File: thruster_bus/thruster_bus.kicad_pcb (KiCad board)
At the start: 2 copper layers, 35.4 x 38.1 mm, 10 parts, among them P1 CONN_01X03, P2 CONN_01X03, P3 CONN_01X03, P4 CONN_01X05, P5 CONN_01X03, P6 CONN_01X03

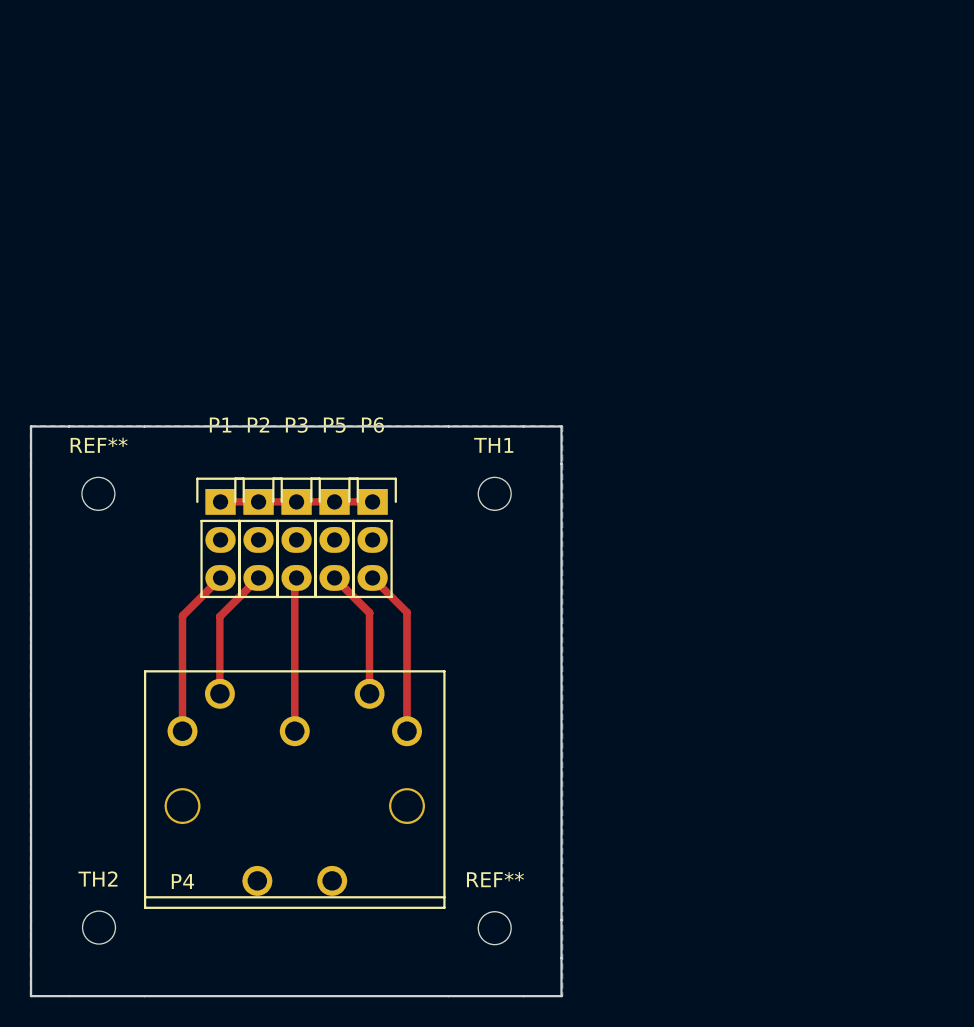
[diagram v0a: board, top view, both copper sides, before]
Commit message: Changed thruster bus pcb to use 6 pin cui connector and to use 5v and GND
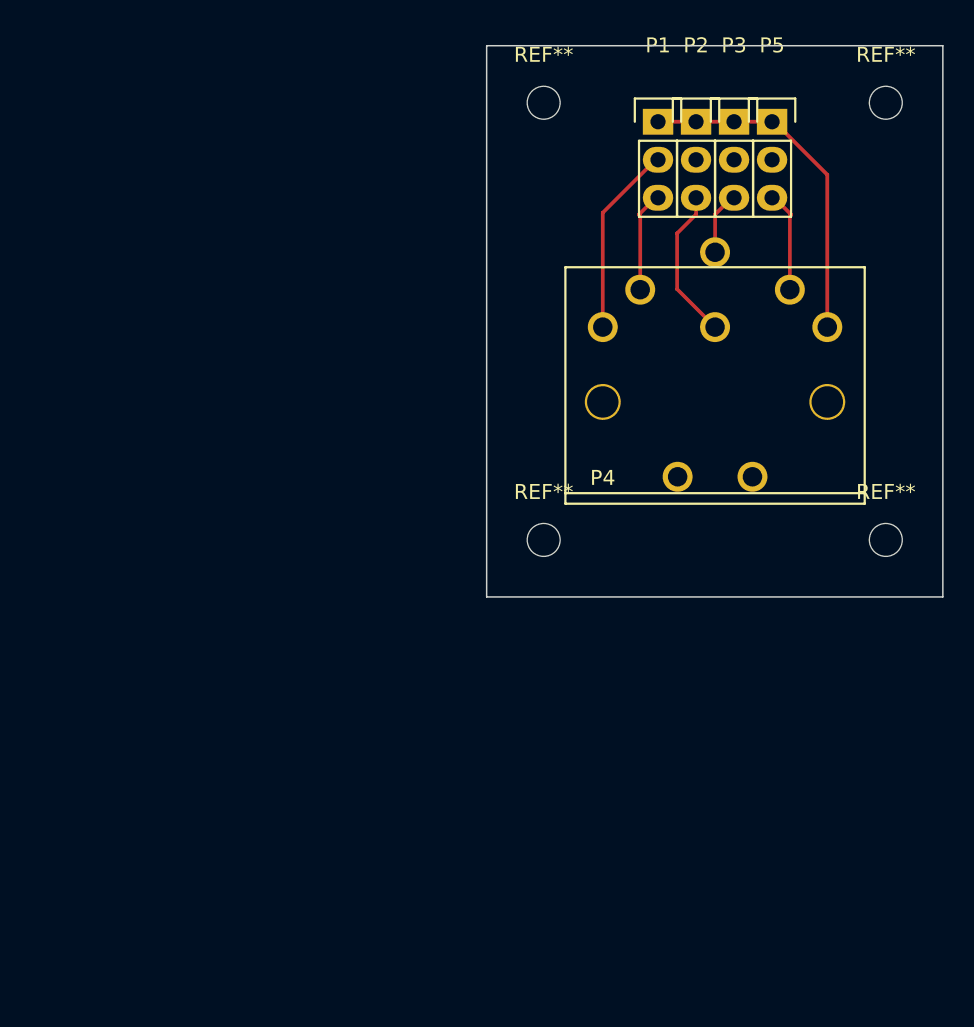
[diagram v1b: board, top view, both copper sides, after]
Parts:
- removed P6: CONN_01X03, Pin_Headers:Pin_Header_Straight_1x03
- removed the REF** at (116.3, 106.1)
- removed the REF** at (142.8, 135.2)
- removed TH1, TH2: MountingHole_2.2mm_M2, Mounting_Holes:MountingHole_2.2mm_M2
- added REF**: MountingHole_2.2mm_M2, Mounting_Holes:MountingHole_2.2mm_M2, F.Cu at (168.9, 109.2)
- added REF**: MountingHole_2.2mm_M2, Mounting_Holes:MountingHole_2.2mm_M2, F.Cu at (146.1, 109.2)
- added REF**: MountingHole_2.2mm_M2, Mounting_Holes:MountingHole_2.2mm_M2, F.Cu at (168.9, 80.0)
- added REF**: MountingHole_2.2mm_M2, Mounting_Holes:MountingHole_2.2mm_M2, F.Cu at (146.1, 80.0)
- P4: value CONN_01X05 -> CONN_01X06; footprint robosub_footprints:cui-5-board-f -> robosub_footprints:cui-6-board-f
- moved P4 39.0 mm to (150.0, 100.0)
- moved P3 38.7 mm to (158.8, 81.3)
- moved P1 38.7 mm to (153.7, 81.3)
- moved P2 38.7 mm to (156.2, 81.3)
- moved P5 38.7 mm to (161.3, 81.3)
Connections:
- P1 pad 2: Net-(P1-Pad2) -> /ESC5V
- P1 pad 3: /3 -> /5
- P2 pad 3: /5 -> /2
- P3 pad 3: /2 -> /6
- P4 pad 1: /1 -> GND
- P4 pad 3: /3 -> /ESC5V
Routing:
- net (no net): track 0.00 -> 30.5 mm
- net /3: track 14.9 -> 0.00 mm
- net /ESC5V: track 0.00 -> 12.8 mm
- net GND: track 10.2 -> 23.0 mm
- net /1: track 11.2 -> 0.00 mm
- net /5: track 12.5 -> 6.79 mm
- net /4: track 12.0 -> 6.79 mm
- net /6: track 0.00 -> 4.26 mm
- removed copper zone on B.Cu, net GND
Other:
- board size 35.4 x 38.1 mm -> 30.5 x 36.8 mm
- net class Default: clearance 0.4 -> 0.2; trace_width 0.5 -> 0.25; via_drill 0.3 -> 0.4
- rule pad_to_mask_clearance: 0.2 -> 0
- rule trace_clearance: 0.4 -> 0.2

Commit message: Addition of labels for OSH Park printing
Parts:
- moved REF** 5.06 mm to (145.0, 104.3)
- moved REF** 5.06 mm to (169.9, 104.3)
- moved REF** 1.53 mm to (145.0, 78.9)
- moved REF** 1.53 mm to (169.9, 78.9)
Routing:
- net (no net): track 30.5 -> 0.00 mm
- net /ESC5V: track 12.8 -> 13.7 mm
- net /2: track 10.2 -> 9.42 mm
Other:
- board size 30.5 x 36.8 mm -> 30 x 30.6 mm
- net class Default: trace_width 0.25 -> 0.758
- board text added: "1"
- board text added: "2"
- board text added: "3"
- board text added: "4"
- board text added: "5"
- board text added: "6"
- board text added: "7"
- board text added: "8"
- board text added: "Case 1"
- board text added: "Case 2"
- board text added: "Thruster Adapter Zachary Pratt RS17"
